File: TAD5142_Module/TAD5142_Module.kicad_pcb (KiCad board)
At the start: 4 copper layers, 40 x 27 mm, 20 parts, among them J1 Conn_01x02, J2 AudioJack2_Ground, J3 Conn_01x05, U1 AP7361EA-33E-13, U2 TAD5142IRGER

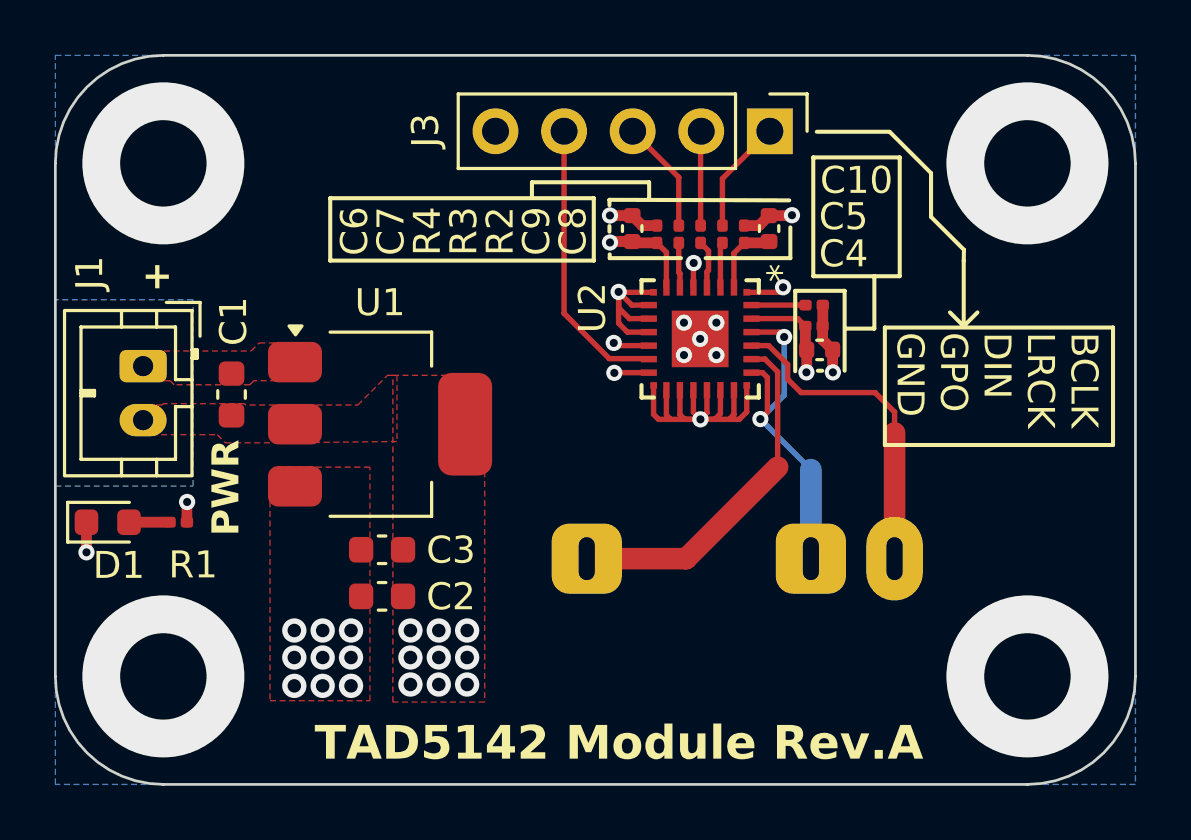
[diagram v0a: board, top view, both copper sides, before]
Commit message: Update TAD5142 module to Revision B
- Update silkscreen text and board metadata to Revision B.
- Adjust PCB edge cuts, dimensions, and mounting hole configuration.
- Correct pad mapping and positioning for the 3.5mm jack (J2).
- Update footprint info cache with Samtec EdgeRate connectors and remove unused hand-soldering variants.
- Add teardrops to several component pads and vias for improved reliability.
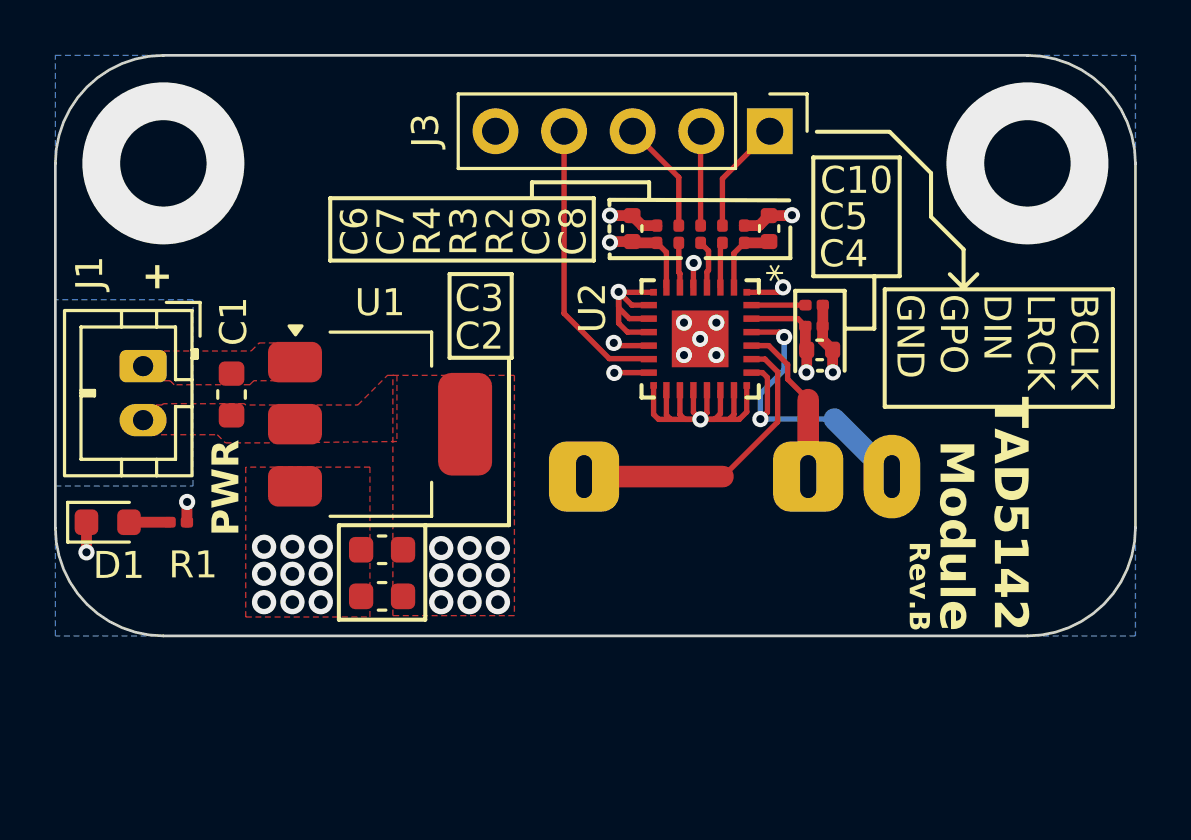
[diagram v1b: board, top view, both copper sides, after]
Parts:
- moved J2 3.04 mm to (152.2, 78.6)
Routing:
- net Net-(U2-OUT2P): track 12.1 -> 6.09 mm
- net Net-(U2-OUT1P): track 13.2 -> 11.0 mm
- net Net-(U2-OUT1M): track 14.4 -> 12.8 mm
- net (no net): vias 4 -> 2
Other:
- board size 40 x 27 mm -> 40 x 21.5 mm
- board text added: "BCLK"
- board text added: "DIN"
- board text added: "GPO"
- board text added: "LRCK"
- board text added: "Rev.B"
- board text added: "TAD5142 Module"
- board text removed: "BCLK LRCK DIN GPO"
- board text removed: "TAD5142 Module Rev.A"
